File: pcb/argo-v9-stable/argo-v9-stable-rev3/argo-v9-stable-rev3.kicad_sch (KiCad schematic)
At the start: 91 parts, among them IC1 MP2672GD, J1 Sparkfun_NEO-N9M-SMA, J2 USB4125-GF-A, J3 LED_power_button_RGB_LED, K1 PRL3-5V-DC-1A, Q2 BSD840N, SW1 POW, U1 orange_pi_zero_2w_2GB, U2 MAX11612, U3 CH221K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

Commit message: rev2 pcb with TODO notes, started on rev3
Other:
- note added: "Add heartbeat (green) LED"
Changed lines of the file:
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@@
+		)
+	)
+	(text "Add heartbeat (green) LED"
+		(exclude_from_sim no)
+		(at 110.49 166.624 0)
+		(effects
+			(font
+				(size 1.27 1.27)
+				(thickness 0.254)
+				(bold yes)
+				(color 255 0 0 1)
+			)
+			(justify left)
 		)
 	)

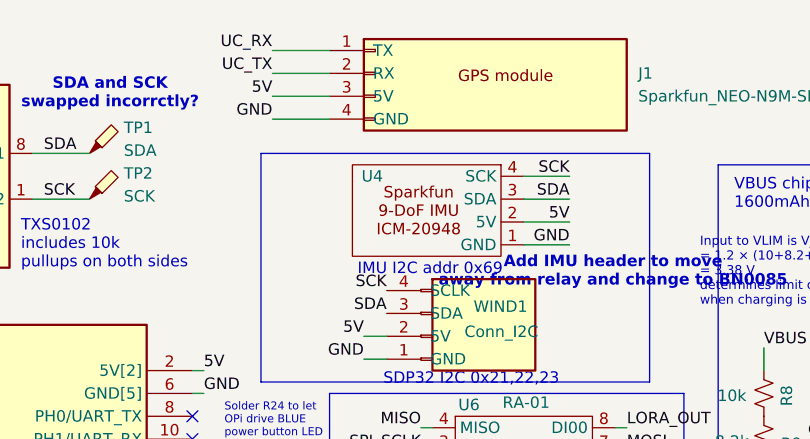
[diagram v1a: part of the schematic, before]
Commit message: more notes about rev3 fixes
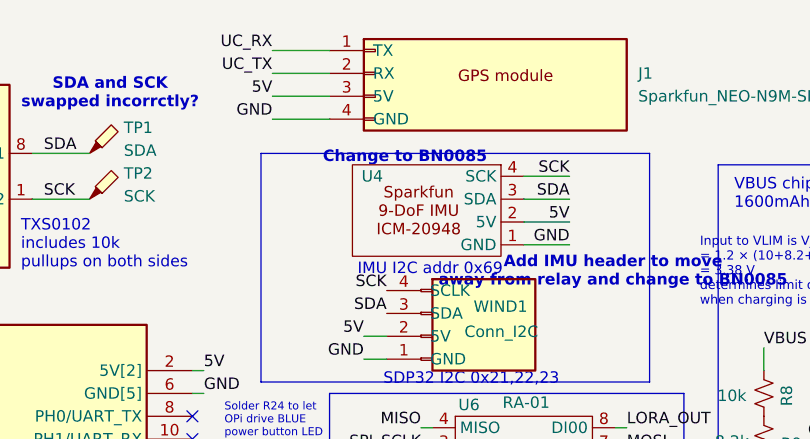
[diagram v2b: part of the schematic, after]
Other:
- note added: "Change to BN0085"
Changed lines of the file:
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@@
+		)
+	)
+	(text "Change to BN0085"
+		(exclude_from_sim no)
+		(at 130.302 28.448 0)
+		(effects
+			(font
+				(size 1.27 1.27)
+				(thickness 0.254)
+				(bold yes)
+				(color 255 0 0 1)
+			)
 		)
 	)

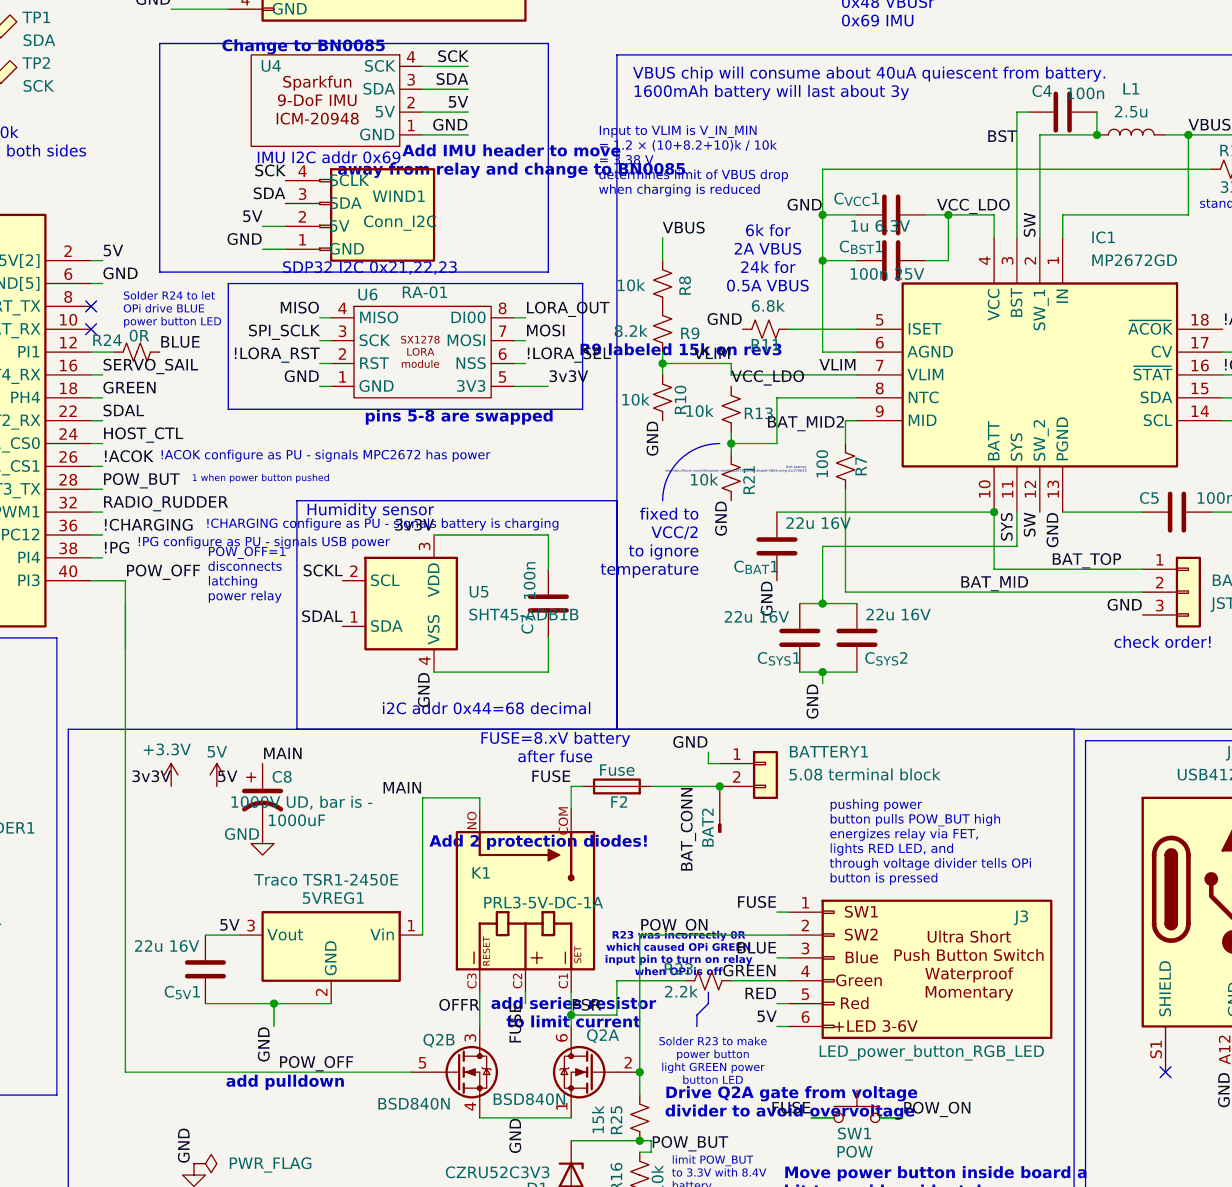
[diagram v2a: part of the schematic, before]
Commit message: schematic, but seems corrupted, might have to roll back
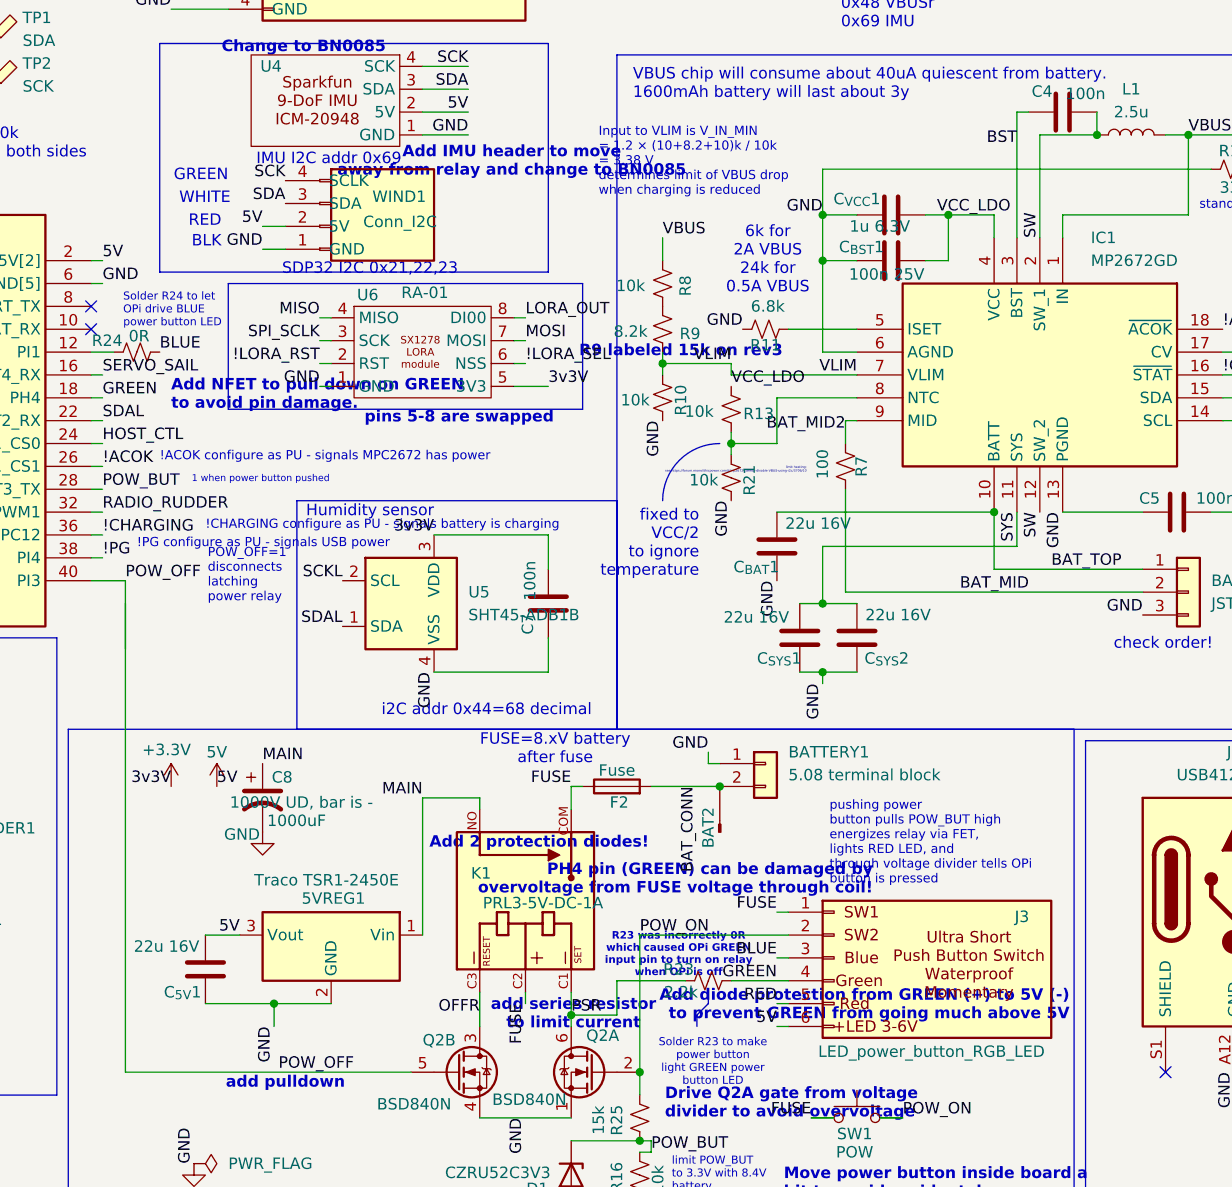
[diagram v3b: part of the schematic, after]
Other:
- note added: "Add NFET to pull down on GREEN to avoid pin damage."
- note added: "Add diode protection from GREEN (+) to 5V (-) to prevent GREEN from going much above 5V"
- note added: "BLK"
- note added: "GREEN"
- note added: "PH4 pin (GREEN) can be damaged by overvoltage from FUSE voltage through coil!"
- note added: "RED"
- note added: "WHITE"
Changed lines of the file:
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@@
+		)
+	)
+	(text "GREEN"
+		(exclude_from_sim no)
+		(at 121.92 42.672 0)
+		(effects
+			(font
+				(size 1.27 1.27)
+				(color 0 255 0 1)
+			)
+			(justify right)
 		)
 	)
@@
 		)
 	)
+	(text "PH4 pin (GREEN) can be damaged by \novervoltage from FUSE voltage through coil!"
+		(exclude_from_sim no)
+		(at 193.548 120.904 0)
+		(effects
+			(font
+				(size 1.27 1.27)
+				(thickness 0.254)
+				(bold yes)
+				(color 255 0 0 1)
+			)
+			(justify right)
+		)
+	)
 	(text "Drive Q2A gate from voltage \ndivider to avoid overvoltage"
 		(exclude_from_sim no)
@@
 		)
 	)
+	(text "Add NFET to pull down on GREEN\nto avoid pin damage."
+		(exclude_from_sim no)
+		(at 115.57 67.056 0)
+		(effects
+			(font
+				(size 1.27 1.27)
+				(thickness 0.254)
+				(bold yes)
+				(color 255 0 0 1)
+			)
+			(justify left)
+		)
+	)
 	(text "wrong fp"
 		(exclude_from_sim no)
@@
 		)
 	)
+	(text "BLK"
+		(exclude_from_sim no)
+		(at 121.158 50.038 0)
+		(effects
+			(font
+				(size 1.27 1.27)
+				(color 0 0 0 1)
+			)
+			(justify right)
+		)
+	)
 	(text "!ACOK configure as PU - signals MPC2672 has power"
 		(exclude_from_sim no)
@@
 		)
 	)
+	(text "WHITE"
+		(exclude_from_sim no)
+		(at 122.174 45.212 0)
+		(effects
+			(font
+				(size 1.27 1.27)
+				(color 194 194 194 1)
+			)
+			(justify right)
+		)
+	)
 	(text "!CHARGING configure as PU - signals battery is charging"
 		(exclude_from_sim no)
@@
 		)
 	)
+	(text "RED"
+		(exclude_from_sim no)
+		(at 121.158 47.752 0)
+		(effects
+			(font
+				(size 1.27 1.27)
+				(color 255 0 0 1)
+			)
+			(justify right)
+		)
+	)
+	(text "Add diode protection from GREEN (+) to 5V (-)\nto prevent GREEN from going much above 5V"
+		(exclude_from_sim no)
+		(at 215.392 134.874 0)
+		(effects
+			(font
+				(size 1.27 1.27)
+				(thickness 0.254)
+				(bold yes)
+				(color 255 0 0 1)
+			)
+			(justify right)
+		)
+	)

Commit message: argo pcb rev3 almost complete
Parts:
- removed 5VREG1: Traco TSR1-2450E, Converter_DCDC:Converter_DCDC_TRACO_TSR1-xxxxE_THT, symbol Regulator_Switching:TSR1-2450E
- removed BAT2: Conn_01x01_Pin, Connector_Pin:Pin_D1.0mm_L10.0mm_LooseFit, symbol Connector:Conn_01x01_Pin
- removed TP1: SDA, Argo footprint Library:TestPoint_scope_probe, symbol Connector:TestPoint_Probe
- removed TP2: SCK, Argo footprint Library:TestPoint_scope_probe, symbol Connector:TestPoint_Probe
- removed TP3: SDAL, Argo footprint Library:TestPoint_scope_probe, symbol Connector:TestPoint_Probe
- removed TP4: SCKL, Argo footprint Library:TestPoint_scope_probe, symbol Connector:TestPoint_Probe
- removed U4: ~, sparkfun:Sparkfun_IMU_ICM-20948, symbol argo-v9:Sparkfun_IMU_ICM-20948
- added D2, D3: TS4148_RCG, Argo footprint Library:DIO_TS4148_RCG, symbol argo-v9:TS4148_RCG
- added Q1: BSD840N, Package_TO_SOT_SMD:SOT-363_SC-70-6, symbol Transistor_FET:BSD840N
- added R33, R34: 10k, Resistor_SMD:R_0603_1608Metric_Pad0.98x0.95mm_HandSolder, symbol Device:R_Small_US
- added TP1, TP10, TP11, TP2, TP3, TP4, TP5, TP6, TP8, TP9: TestPoint_Probe_autonamed, Argo footprint Library:TestPoint_scope_probe_autonamed, symbol argo-v9:TestPoint_Probe_autonamed
- added U4: ~, Argo footprint Library:I2C_header, symbol argo-v9:Adafruit_BNO085
- added U8: TSR_1-2450, Argo footprint Library:Converter_DCDC_TRACO_TSR1-xxxxE_THT, symbol argo-v9:TSR_1-2450
- C1: value 100n -> 10uF
- D1: footprint Diode_SMD:D_MiniMELF -> Argo footprint Library:D_0603_1608Metric_hand_solder
- J3: footprint Connector_JST:JST_XH_B6B-XH-AM_1x06_P2.50mm_Vertical -> Argo footprint Library:JST_XH_B6B-XH-AM_1x06_P2.50mm_Vertical
- K1: footprint PRL3-5V-DC-1A:RELAY_PRL3-5V-DC-1A -> Argo footprint Library:RELAY_PRL3-5V-DC-1A
- Q2: footprint Package_TO_SOT_SMD:SOT-363_SC-70-6 -> Argo footprint Library:SOT-363_SC-70-6-handsolder
- R1: value 1M -> 150k
- U1: footprint orangepi-zero:orange_pi_zero_2w -> Argo footprint Library:orange_pi_zero_2w_butted
- U5: footprint Sensor_Humidity:Sensirion_DFN-4_1.5x1.5mm_P0.8mm_SHT4x_NoCentralPad -> Argo footprint Library:Sensirion_DFN-4_1.5x1.5mm_P0.8mm_SHT4x_NoCentralPad-handsolder
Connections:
- net POW_ON is gone; now on net POW_BUT: J3.2 (Pin_2), POW_BUT1.2 (A), Q2.2 (G), R25.2, SW1.2
- net !LORA_SEL: now also U6.7 (NSS); no longer U6.6 (NSS)
- net +3.3V: now also U6.8 (3V3); no longer U6.5 (3V3)
- net 5V: now also WIND1.3 (5V), U4.2 (5V), U8.3 (Vout); no longer WIND1.2 (5V)
- net BAT_MID2: now also TP8.1
- net BAT_TOP: now also TP9.1
- net FUSE: now also D2.C, D3.C
- net GND: now also WIND1.4 (GND), Q1.4 (S), R33.2, R34.1, U4.1 (GND), U8.2 (GND); no longer WIND1.1 (GND)
- net GREEN: now also Q1.3 (D); no longer U1.18 (PH4)
- net HOST_CTL: no longer R32.2
- net LORA_OUT: now also U6.5 (DI00); no longer U6.8 (DI00)
- net MAIN: now also U8.1 (Vin)
- net MOSI: now also U6.6 (MOSI); no longer U6.7 (MOSI)
- net OFFR: now also D2.A
- net POW_BUT: now also TP6.1
- net POW_OFF: now also R33.1
- net PSR: now also D3.A
- net SCK: now also U7.8 (B1), WIND1.1 (SCLK), TP1.1, U4.4 (SCK); no longer U7.1 (B2), WIND1.4 (SCLK)
- net SCKL: now also TP3.1
- net SDA: now also U7.1 (B2), WIND1.2 (SDA), TP2.1, U4.3 (SDA); no longer U7.8 (B1), WIND1.3 (SDA)
- net SDAL: now also TP4.1
- net VBUS: now also TP11.1, TP5.1
- net VCC_LDO: now also R32.2
- net VLIM: now also TP10.1
- new net PH4: Q1.5 (G), R34.2, U1.18 (PH4)
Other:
- note added: "Add RESET and SAFEBOOT GPIO outputs to reset or safe boot"
- note added: "Check !CHARGING when OPi running, might need pullup or pulldown"
- note added: "Diodes protect FET drains when relay coils turn off and create voltage spike above FUSE=battery"
- note added: "Fully charged battery makes 8.4V. Rtop=27k Rbot=18k, then vout=0.4vin, so 8.4V will give 3.36V"
- note added: "I2C addressses 0x21,0x22,0x23 wind 0x34 ADC 0x44 humidity 0x48 MP2672 charger (if configured) 0x69 IMU"
- note added: "LORA long range radio"
- note added: "MAIN=battery after relay"
- note added: "R12: standalone solder for standalone"
- note added: "R1=150k and C1=10uF are suitable for sponge saturated with salt"
- note added: "R32: Solder for host controlled, do not solder for standalone Host-controlled does not work with OPi can be off. See https://forum.monolithicpower.com/t/mp2672-i2c-comms-with-power-disconnected/1952/11"
- note added: "Winch servo requires smaller resistor to override radio output"
- note added: "holds relay coil off even if OPi is off"
- note removed: "Add 2 protection diodes!"
- note removed: "Add IMU header to move away from relay and change to BN0085"
- note removed: "Add NFET to pull down on GREEN to avoid pin damage."
- note removed: "Add diode protection from GREEN (+) to 5V (-) to prevent GREEN from going much above 5V"
- note removed: "Change to BN0085"
- note removed: "Drive Q2A gate from voltage divider to avoid overvoltage"
- note removed: "Fully VBUSd 2S makes 8.4V. Rtop=27k Rbot=18k, then vout=0.4vin, so 8.4V will give 3.36V"
- note removed: "I2C addressses 0x21,0x22,0x23 wind 0x34 ADC 0x44 humidity 0x48 VBUSr 0x69 IMU"
- note removed: "Move power button inside board a bit to avoid accidental power ons"
- note removed: "PH4 pin (GREEN) can be damaged by overvoltage from FUSE voltage through coil!"
- note removed: "R23 was incorrectly 0R which caused OPi GREEN input pin to turn on relay when OPi is off"
- note removed: "R28 and R29 are inorrectly 0R; they should be 5.1k"
- note removed: "R32: Solder for host controlled, do not solder for standalone"
- note removed: "R9 labeled 15k on rev3"
- note removed: "SDA and SCK swapped incorrctly?"
- note removed: "add pulldown"
- note removed: "add series resistor to limit current"
- note removed: "incorrect on pcb as 10k"
- note removed: "pins 5-8 are swapped"
- note removed: "standalone"
- note removed: "wrong fp"
- moved on the sheet: 3v3v1, 5V1, BAT1, BATTERY1, BAT_BAL1, C1, C2, C3, C4, C5, C6, C7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
